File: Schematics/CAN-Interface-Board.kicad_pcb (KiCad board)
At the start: 4 copper layers, 50 x 100 mm, 78 parts, among them CN1 Limit Switch Connector 1, CN2 Limit Switch Connector 2, CN3 XY-B3B-XH-A, CN4 XY-B3B-XH-A, J1 Microsemi_FlashPro-JTAG-10, J2 USB_C_Receptacle, J3 Micro_SD_Card, Q1 INA180A2, U1 SN65HVD230, U2 LDL1117-3.3, U3 STM32F405RGT6, U4 MPL3115A2R1, U5 LSM6DS3TR-C, U6 TPS22917DBVR, Y1 8mhz

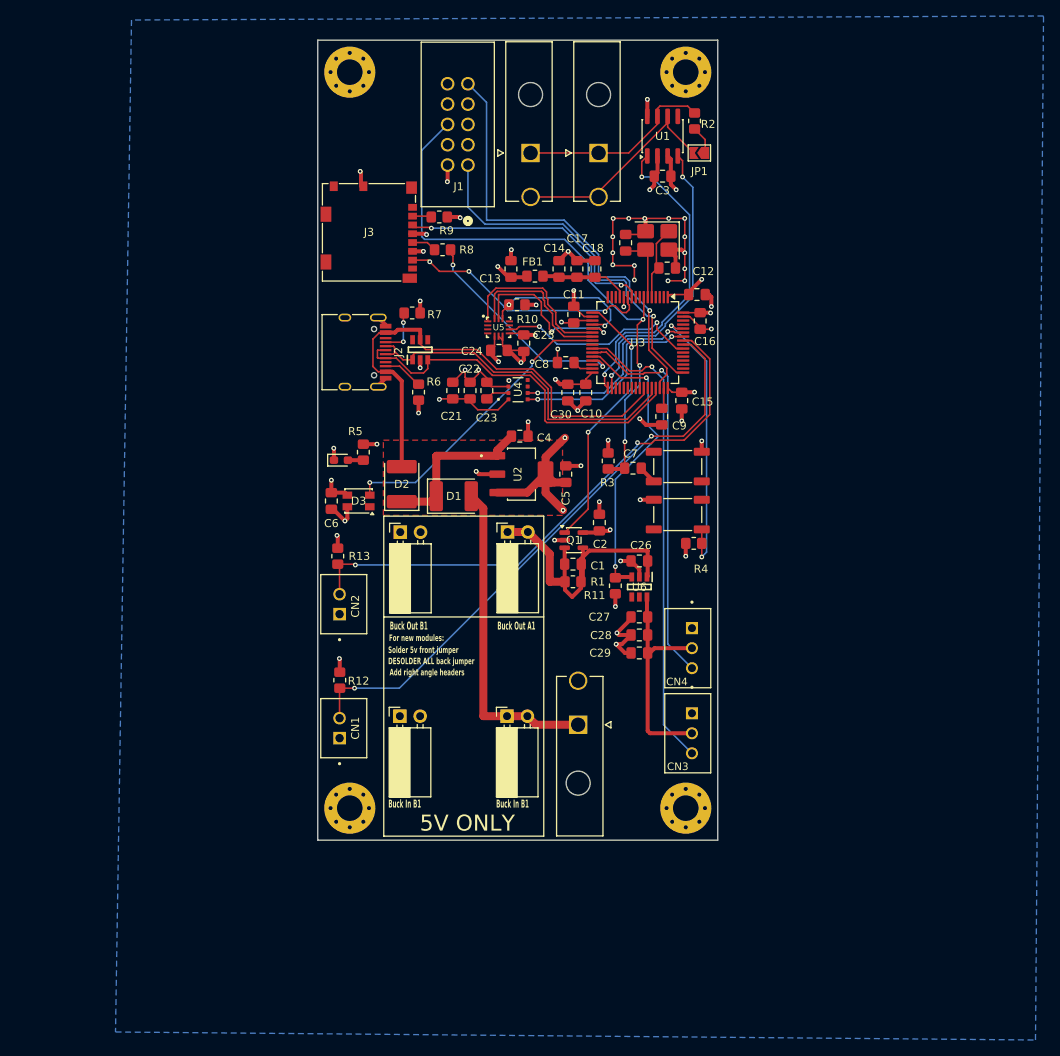
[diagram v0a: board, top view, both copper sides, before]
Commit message: started new design with esp32
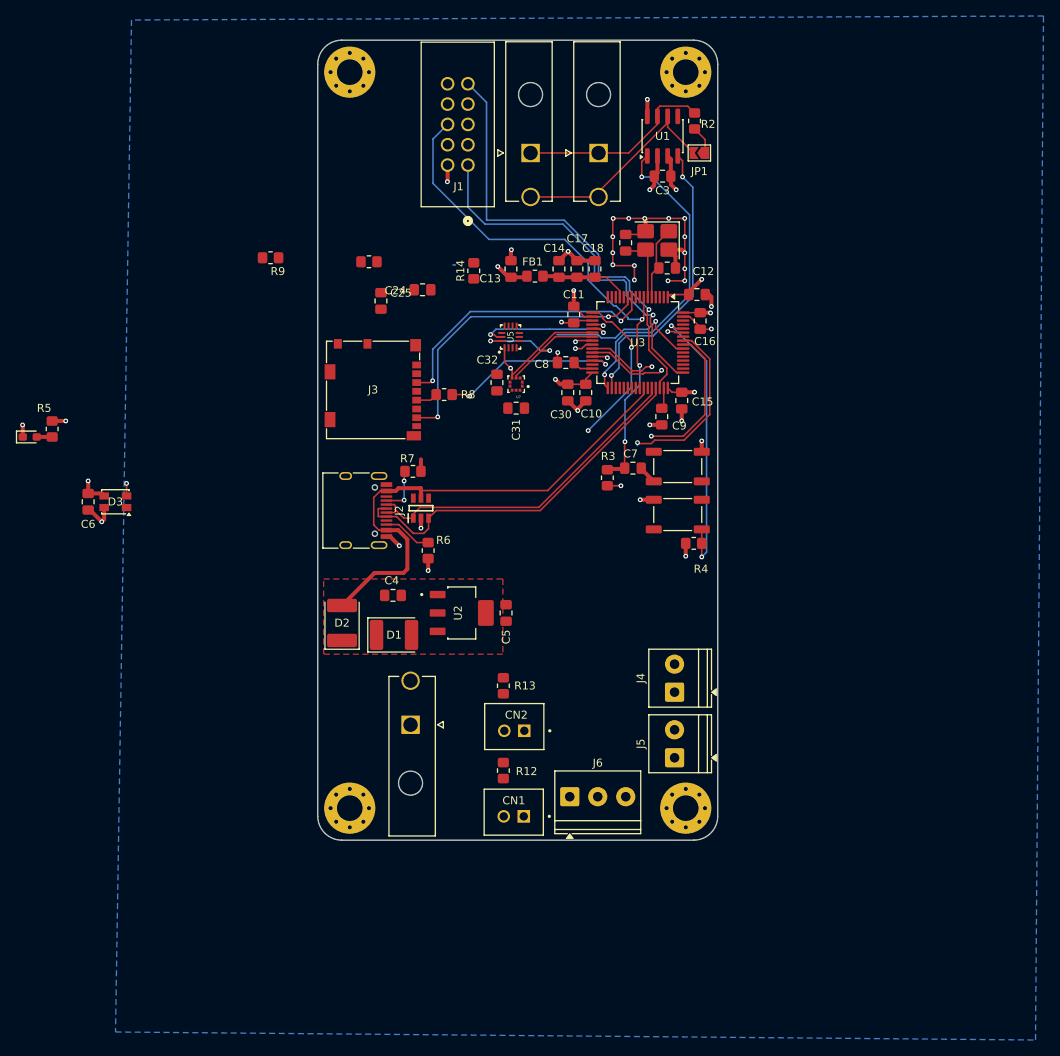
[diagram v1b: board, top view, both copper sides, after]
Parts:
- removed C1, C2, C21, C22, C23, C27: 100nf, Capacitor_SMD:C_0805_2012Metric_Pad1.18x1.45mm_HandSolder
- removed C26, C28: 1uf, Capacitor_SMD:C_0805_2012Metric_Pad1.18x1.45mm_HandSolder
- removed C29: 47uf, Capacitor_SMD:C_0805_2012Metric_Pad1.18x1.45mm_HandSolder
- removed CN3, CN4: XY-B3B-XH-A, myFootprints:JST_B3B-XH-A
- removed J_BUCK_IN_A1, J_BUCK_IN_B1, J_BUCK_OUT_A1, J_BUCK_OUT_B1: ~, Connector_PinSocket_2.54mm:PinSocket_1x02_P2.54mm_Horizontal
- removed Q1: INA180A2, Package_TO_SOT_SMD:SOT-23-5
- removed R1: 150r, Resistor_SMD:R_0805_2012Metric_Pad1.20x1.40mm_HandSolder
- removed R11: 100k, Resistor_SMD:R_0805_2012Metric_Pad1.20x1.40mm_HandSolder
- removed U4: MPL3115A2R1, myFootprints:PSON80P300X300X100-8N
- removed U6: TPS22917DBVR, myFootprints:SOT95P280X145-6N
- added C31: 100nf, Capacitor_SMD:C_0805_2012Metric_Pad1.18x1.45mm_HandSolder, F.Cu at (134.8, 76.0)
- added C32: 100nf, Capacitor_SMD:C_0805_2012Metric_Pad1.18x1.45mm_HandSolder, F.Cu at (132.4, 72.8)
- added J4: Screw_Terminal_01x02, TerminalBlock_Phoenix:TerminalBlock_Phoenix_PT-1,5-2-3.5-H_1x02_P3.50mm_Horizontal, F.Cu at (154.6, 111.5)
- added J5: Screw_Terminal_01x02, TerminalBlock_Phoenix:TerminalBlock_Phoenix_PT-1,5-2-3.5-H_1x02_P3.50mm_Horizontal, F.Cu at (154.6, 119.7)
- added J6: Screw_Terminal_01x03, TerminalBlock_Phoenix:TerminalBlock_Phoenix_PT-1,5-3-3.5-H_1x03_P3.50mm_Horizontal, F.Cu at (141.5, 124.6)
- added R14: 10k, Resistor_SMD:R_0805_2012Metric_Pad1.20x1.40mm_HandSolder, F.Cu at (129.5, 58.8)
- added U7: Bosch BMP388, myFootprints:PQFN50P200X200X80-10N, F.Cu at (134.8, 73.0)
- moved PowerLED1 39.0 mm to (74.0, 79.6)
- moved R5 39.0 mm to (76.8, 78.6)
- moved C6 30.4 mm to (81.3, 87.7)
- moved D3 30.4 mm to (84.7, 87.7)
- moved R13 26.3 mm to (133.2, 110.7)
- moved CN2 26.2 mm to (134.6, 115.8), turned to 0 degrees
- moved C4 25.4 mm to (119.4, 99.4)
- moved CN1 23.7 mm to (134.5, 126.5), turned to 0 degrees
- moved R12 23.4 mm to (133.2, 121.3)
- moved R9 21.7 mm to (104.1, 57.2)
- moved PowerIn1 21.0 mm to (121.6, 115.6)
- moved R6 19.8 mm to (123.8, 93.8)
- moved R7 19.8 mm to (121.9, 83.9)
- moved D4 19.8 mm to (122.9, 88.5)
- moved J2 19.8 mm to (114.5, 88.8)
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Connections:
- net /IMU/IMU_MISO renamed /Barometer/Baraometer-MISO
- net /IMU/IMU_MOSI renamed /Barometer/Baraometer-MOSI
- net /IMU/IMU_SCK renamed /Barometer/Baraometer-SCK
- U3 pad 17: /Current Sensor/VoltageADC -> /MCU/CurrentCheck
- U3 pad 25: unconnected-(U3-PC5-Pad25) -> /Barometer/Baraometer-ChipSelect
- U3 pad 58: /Barometer/BarometerSCL -> unconnected-(U3-PB6-Pad58)
- U3 pad 59: /Barometer/BarometerSDA -> unconnected-(U3-PB7-Pad59)
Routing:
- net /MCU/LimitSwitchCAS: track 74.0 -> 18.3 mm, vias 2 -> 1
- net GND: track 137.6 -> 85.3 mm, vias 49 -> 33
- net /MCU/PWMServo_Roll: track 59.2 -> 8.80 mm
- net +3.3V: track 90.4 -> 42.1 mm, vias 23 -> 12
- net /MCU/LimitSwitchRoll: track 69.7 -> 22.2 mm, vias 2 -> 1
- net +BATT: track 40.4 -> 0.00 mm
- net +5V: track 40.0 -> 0.00 mm
- net /MCU/PWMServo_CAS: track 48.8 -> 9.95 mm
- net /MCU/5Venable: track 37.9 -> 1.94 mm, vias 2 -> 1
- net /Current Sensor/VoltageADC: track 33.4 -> 0.00 mm, vias 2 -> 0
- net /MCU/RGB_DATA: track 37.0 -> 3.75 mm
- net /Servo/<NO NET>: track 28.2 -> 0.00 mm
- net /Barometer/BarometerSDA: track 25.0 -> 0.00 mm, vias 2 -> 0
- net /Barometer/BarometerSCL: track 24.9 -> 0.00 mm, vias 2 -> 0
- net Net-(D1-K): track 20.5 -> 0.00 mm
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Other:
- outline, holes or cut-outs redrawn
- board text removed: "5V ONLY"
- board text removed: "Add right angle headers"
- board text removed: "Buck In B1"
- board text removed: "Buck Out A1"
- board text removed: "Buck Out B1"
- board text removed: "DESOLDER ALL back jumper"
- board text removed: "For new modules:"
- board text removed: "Solder 5v front jumper"

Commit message: added esp32 for uart to tune control systems from a web browser app
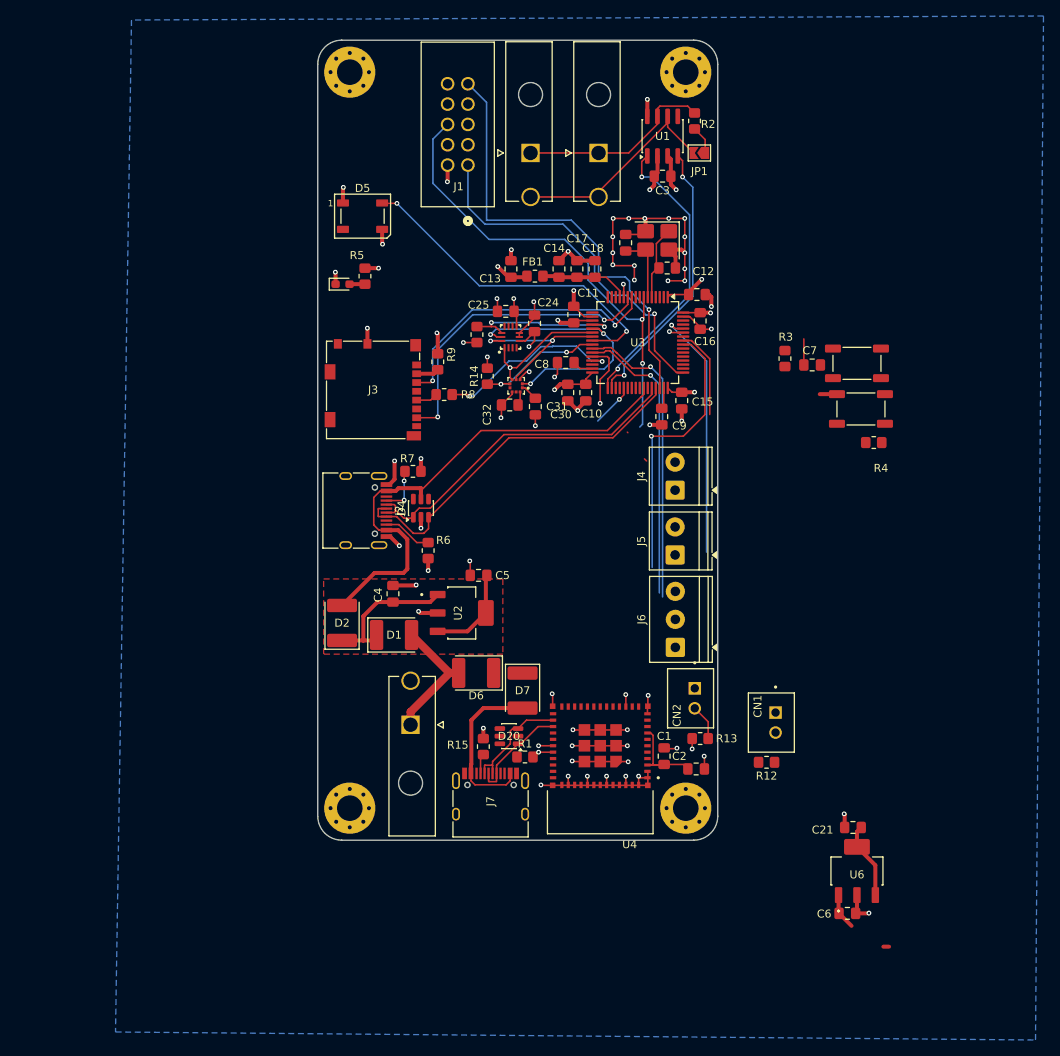
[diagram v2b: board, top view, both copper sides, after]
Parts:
- removed D3: NeoPixel_THT, LED_SMD:LED_Kingbright_AAA3528ESGCT
- added C1: 100nf, Capacitor_SMD:C_0805_2012Metric_Pad1.18x1.45mm_HandSolder, F.Cu at (153.3, 119.5)
- added C2: 1uf, Capacitor_SMD:C_0805_2012Metric_Pad1.18x1.45mm_HandSolder, F.Cu at (157.3, 121.1)
- added C21: 4.7u, Capacitor_SMD:C_0805_2012Metric_Pad1.18x1.45mm_HandSolder, F.Cu at (176.9, 128.4)
- added D20: SRV05-4.TCT, Package_TO_SOT_SMD:SOT-23-6, F.Cu at (133.9, 117.0)
- added D5: ws2812b, LED_SMD:LED_WS2812B_PLCC4_5.0x5.0mm_P3.2mm, F.Cu at (115.6, 52.0)
- added D6: D_Schottky, Diode_SMD:D_2114_3652Metric, F.Cu at (129.8, 109.1)
- added D7: D_Schottky, Diode_SMD:D_2114_3652Metric, F.Cu at (135.6, 111.3)
- added J7: USB_C_Receptacle, Connector_USB:USB_C_Receptacle_HRO_TYPE-C-31-M-12, F.Cu at (131.6, 125.7)
- added R1: 5.1k, Resistor_SMD:R_0805_2012Metric_Pad1.20x1.40mm_HandSolder, F.Cu at (135.9, 119.6)
- added R15: 5.1k, Resistor_SMD:R_0805_2012Metric_Pad1.20x1.40mm_HandSolder, F.Cu at (130.7, 118.3)
- added U4: ESP32-C3-MINI-1-N4, myFootprints:XCVR_ESP32-C3-MINI-1-N4, F.Cu at (145.3, 120.9)
- added U6: LDL1117-3.3, myFootprints:SOT230P700X180-4N, F.Cu at (177.4, 133.8)
- C6: value 100nf -> 1u
- D4: footprint myFootprints:SOT95P280X145-6N -> Package_TO_SOT_SMD:SOT-23-6
- moved C6 107.9 mm to (176.2, 139.2), turned to 0 degrees
- moved R5 43.5 mm to (115.9, 59.5)
- moved PowerLED1 43.5 mm to (113.1, 60.5)
- moved CN1 34.1 mm to (166.7, 115.3), turned to 90 degrees
- moved R12 32.9 mm to (166.1, 120.3), turned to 0 degrees
- moved R3 26.7 mm to (168.4, 69.8)
- moved BootSwitch1 26.4 mm to (177.9, 76.1)
- moved C7 25.8 mm to (171.8, 70.6)
- moved RSTSwitch1 25.8 mm to (177.4, 70.4)
- moved R4 25.8 mm to (179.5, 80.3)
- moved R13 25.5 mm to (157.8, 117.3), turned to 0 degrees
- moved J5 25.4 mm to (154.7, 94.3)
- moved J4 25.3 mm to (154.7, 86.2)
- moved R9 24.6 mm to (125.0, 70.2), turned to -90 degrees
- moved J6 22.9 mm to (154.7, 105.9), turned to 90 degrees
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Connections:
- C6 pad 1: GND -> Net-(D6-K)
- C6 pad 2: +3.3V -> GND
- J2 pad S1: GND -> unconnected-(J2-SHIELD-PadS1)_3
- U3 pad 17: /MCU/CurrentCheck -> unconnected-(U3-PA3-Pad17)
- U3 pad 37: unconnected-(U3-PC6-Pad37) -> /MCU/CurrentCheck
- U3 pad 55: /IMU/IMU_DReady -> unconnected-(U3-PB3-Pad55)
- U5 pad 9: /IMU/IMU_DReady -> unconnected-(U5-INT2-Pad9)
- U7 pad 2: (no net) -> /Barometer/Baraometer-SCK
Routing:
- net GND: track 85.3 -> 168.7 mm, vias 33 -> 64
- net /MCU/RGB_DATA: track 3.75 -> 42.1 mm
- net /MCU/PWMServo_Roll: track 8.80 -> 38.0 mm
- net +3.3V: track 42.1 -> 69.3 mm, vias 12 -> 15
- net /MCU/PWMServo_CAS: track 9.95 -> 36.3 mm
- net /ESP32-C3-Mini/ESPPower: track 0.00 -> 22.2 mm
- net /ESP32-C3-Mini/ESP5vUSB: track 0.00 -> 20.9 mm
- net /IMU/IMU_DReady: track 18.7 -> 0.00 mm, vias 1 -> 0
- net /IMU/IMU_CS: track 1.42 -> 19.9 mm, vias 1 -> 2
- net Net-(D1-K): track 0.00 -> 18.0 mm
- net /Barometer/Baraometer-SCK: track 17.7 -> 34.3 mm, vias 2 -> 3
- net /MCU/LimitSwitchCAS: track 18.3 -> 34.7 mm
- net +BATT: track 0.00 -> 16.3 mm
- net /MCU/CurrentCheck: track 19.9 -> 5.47 mm, vias 2 -> 1
- net /ESP32-C3-Mini/D-: track 0.00 -> 14.1 mm
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
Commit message: finished first layout and routing
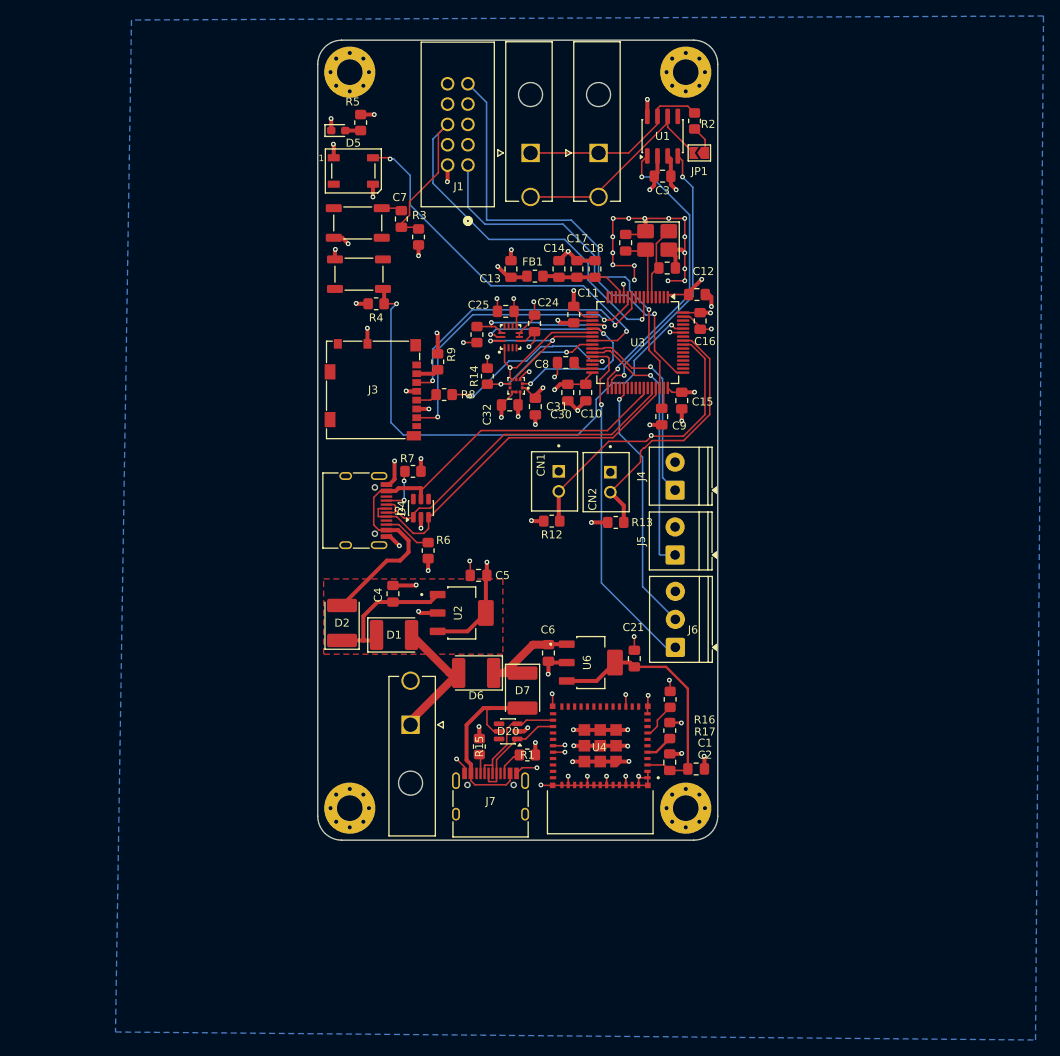
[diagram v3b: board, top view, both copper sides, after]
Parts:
- added R16: 10k, Resistor_SMD:R_0805_2012Metric_Pad1.20x1.40mm_HandSolder, F.Cu at (154.1, 112.4)
- added R17: 10k, Resistor_SMD:R_0805_2012Metric_Pad1.20x1.40mm_HandSolder, F.Cu at (154.0, 116.3)
- moved BootSwitch1 65.0 mm to (115.2, 59.2)
- moved RSTSwitch1 64.8 mm to (115.0, 52.9), turned to 0 degrees
- moved R4 64.6 mm to (117.3, 63.0)
- moved C7 54.5 mm to (120.5, 52.4), turned to 90 degrees
- moved C6 49.6 mm to (138.8, 106.6), turned to -90 degrees
- moved R3 48.3 mm to (122.6, 54.6)
- moved U6 42.3 mm to (144.1, 107.8), turned to 0 degrees
- moved CN1 40.5 mm to (139.6, 85.2)
- moved R12 40.4 mm to (139.2, 90.1)
- moved C21 34.5 mm to (149.6, 107.3), turned to 90 degrees
- moved R13 29.0 mm to (147.2, 90.3)
- moved CN2 29.0 mm to (146.1, 85.2)
- moved PowerLED1 19.2 mm to (112.6, 41.3)
- moved R5 19.2 mm to (115.4, 40.3)
- moved D5 5.77 mm to (114.5, 46.4)
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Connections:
- D20 pad 5: /ESP32-C3-Mini/USB5V -> /ESP32-C3-Mini/ESP5vUSB
- U4 pad 5: unconnected-(U4-IO2-Pad5) -> Net-(U4-IO2)
- U4 pad 8: /ESP32-C3-Mini/ESPPower -> /ESP32-C3-Mini/STM-ESP-ON
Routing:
- net /MCU/5Venable: track 8.27 -> 43.4 mm
- net /MCU/BOOT0: track 31.8 -> 63.9 mm, vias 1 -> 2
- net /MCU/CurrentCheck: track 5.47 -> 32.1 mm
- net GND: track 168.7 -> 186.3 mm, vias 64 -> 73
- net /MCU/LimitSwitchRoll: track 15.7 -> 33.0 mm
- net /MCU/PWMServo_Roll: track 38.0 -> 25.2 mm
- net /ESP32-C3-Mini/ESPPower: track 22.2 -> 32.9 mm
- net Net-(D6-K): track 5.23 -> 13.6 mm
- net +3.3V: track 69.3 -> 77.1 mm, vias 15 -> 22
- net /MCU/RGB_DATA: track 42.1 -> 47.8 mm
- net /ESP32-C3-Mini/ESP5vUSB: track 20.9 -> 25.5 mm
- net /ESP32-C3-Mini/STM-ESP-ON: track 0.00 -> 4.61 mm
- net Net-(U4-IO2): track 0.00 -> 3.49 mm
- net Net-(J7-CC2): track 0.00 -> 2.94 mm
- net /MCU/PWMServo_CAS: track 36.3 -> 33.4 mm
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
